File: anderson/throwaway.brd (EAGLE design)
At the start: 45.7 x 30.5 mm, 5 parts

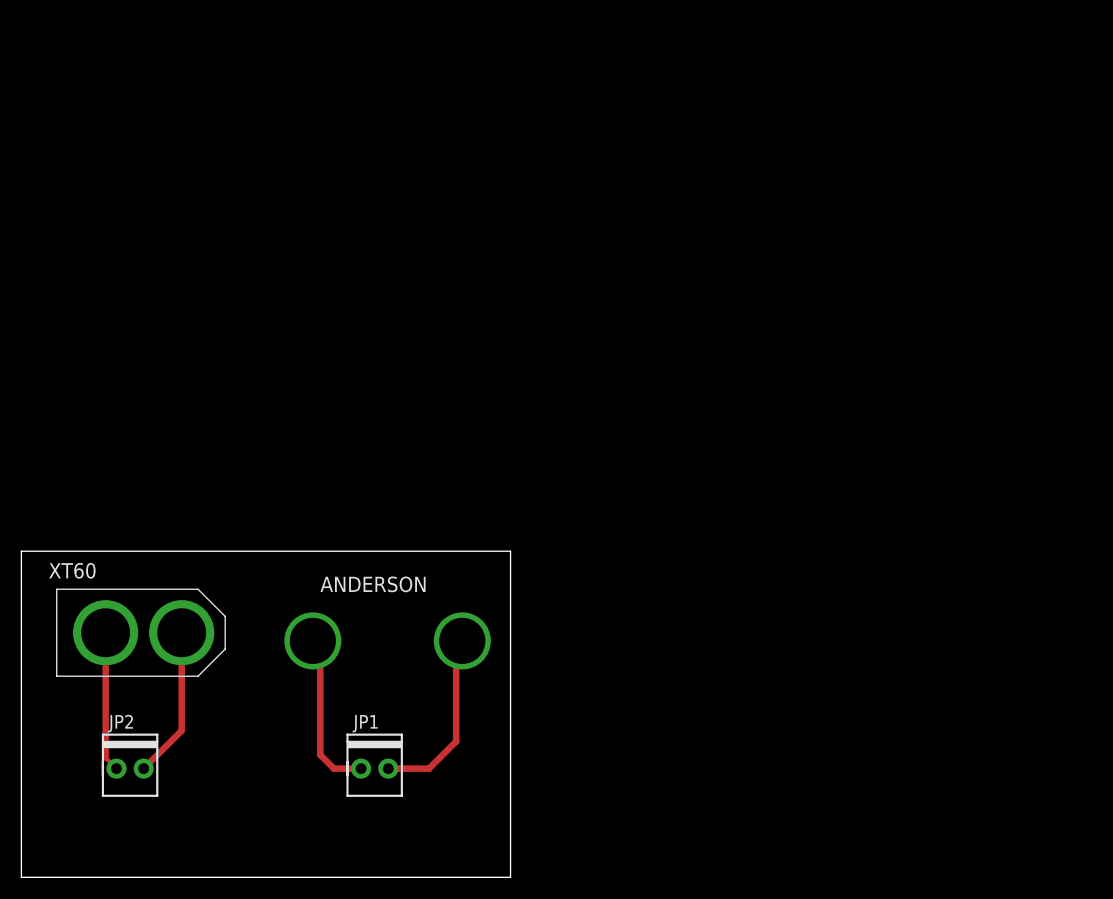
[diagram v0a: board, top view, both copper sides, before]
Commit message: Anderson Throwaways
25 Amp Andersons on throwaway boards with XT60 connectors.
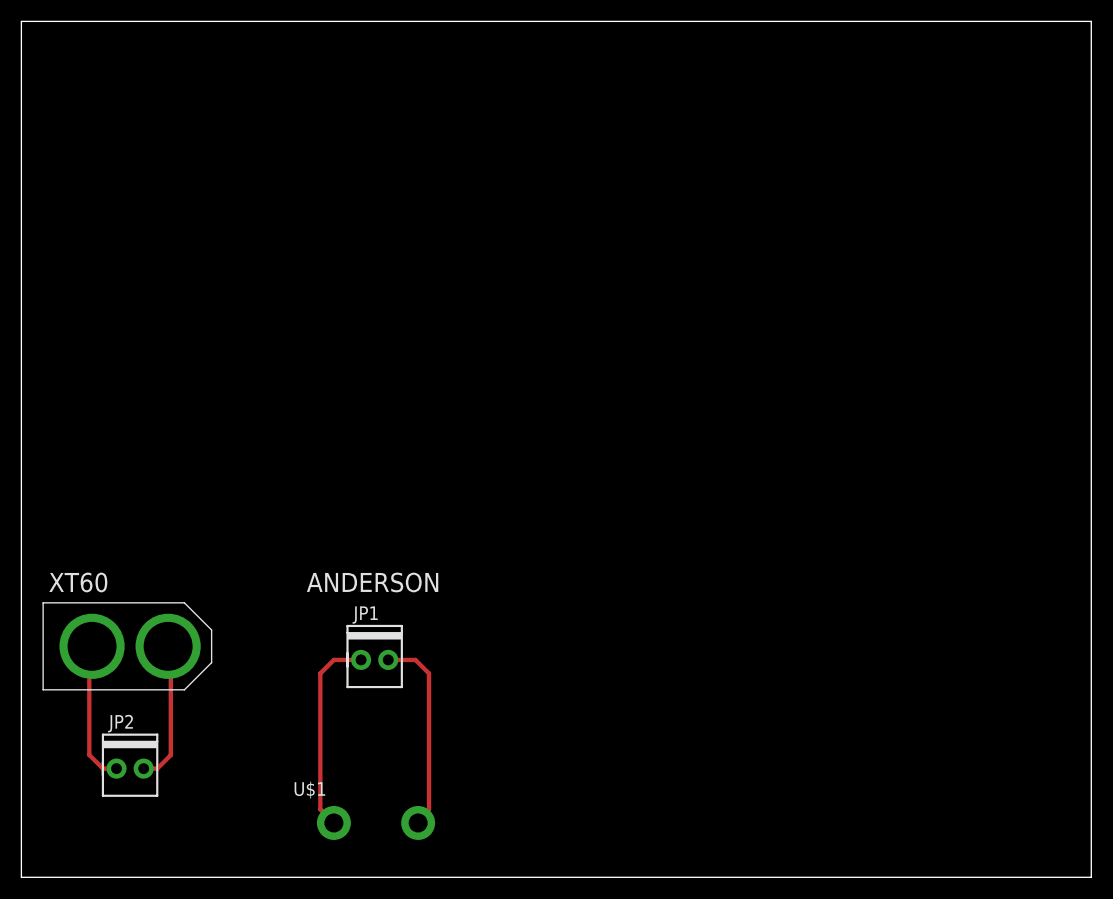
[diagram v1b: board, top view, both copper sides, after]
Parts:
- removed U$2: ANDERSON_RA_BOTTOM, pie:ANDERSON_RA_BOTTOM
- U$1: value ANDERSON_RA_BOTTOM -> ANDERSON_25A_1X2; device pie:ANDERSON_RA_BOTTOM -> pie:ANDERSON_25A_1X2
- moved U$1 16.9 mm to (29.2, 5.08)
- moved JP1 10.2 mm to (33.0, 20.3)
- moved U$3 1.80 mm to (10.2, 21.6)
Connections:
- net N$2: now also U$1.PIN2; no longer U$2.PIN1
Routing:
- net N$1: track 15.3 -> 18.8 mm
- net N$2: track 17.0 -> 18.8 mm
- net N$3: track 14.2 -> 13.2 mm
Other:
- board size 45.7 x 30.5 mm -> 100 x 80 mm

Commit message: Anderson Throwaway
Replaced wrong anderson on throwaway with correct 25A andersons
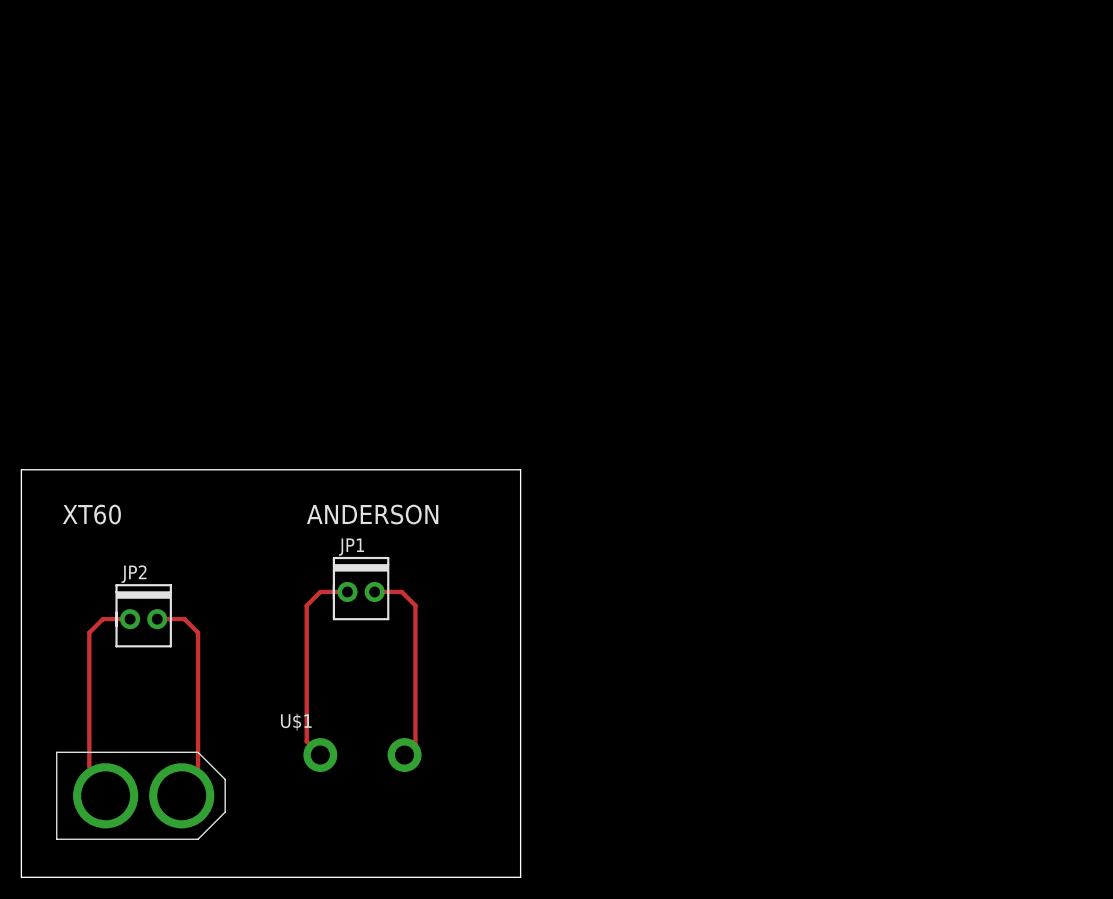
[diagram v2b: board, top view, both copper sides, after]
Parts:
- moved JP2 14.0 mm to (11.4, 24.1)
- moved U$3 14.0 mm to (11.4, 7.62)
- moved JP1 6.48 mm to (31.8, 26.7)
- moved U$1 6.48 mm to (27.9, 11.4)
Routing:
- net N$3: track 13.2 -> 20.2 mm
- net N$4: track 13.2 -> 20.2 mm
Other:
- board size 100 x 80 mm -> 46.7 x 38.1 mm
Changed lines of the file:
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@@
 <board>
 <plain>
-<wire x1="0" y1="0" x2="100" y2="0" width="0" layer="20"/>
-<wire x1="100" y1="0" x2="100" y2="80" width="0" layer="20"/>
-<wire x1="100" y1="80" x2="0" y2="80" width="0" layer="20"/>
-<wire x1="0" y1="80" x2="0" y2="0" width="0" layer="20"/>
-<text x="2.54" y="26.67" size="1.778" layer="25" font="vector">XT60</text>
-<text x="26.67" y="26.67" size="1.778" layer="25" font="vector">ANDERSON</text>
+<wire x1="0" y1="0" x2="46.66" y2="0" width="0" layer="20"/>
+<wire x1="46.66" y1="0" x2="46.66" y2="38.09" width="0" layer="20"/>
+<wire x1="46.66" y1="38.09" x2="0" y2="38.09" width="0" layer="20"/>
+<wire x1="0" y1="38.09" x2="0" y2="0" width="0" layer="20"/>
+<text x="3.81" y="33.02" size="1.778" layer="25" font="vector">XT60</text>
+<text x="26.67" y="33.02" size="1.778" layer="25" font="vector">ANDERSON</text>
 </plain>
 <attributes>
@@
 </autorouter>
 <elements>
-<element name="JP1" library="pie" package="1X02-MTA" value="" x="33.02" y="20.32">
-<attribute name="PARTNUMBER" value="A1921-ND" x="66.04" y="11.43" size="1.778" layer="27" display="off"/>
+<element name="JP1" library="pie" package="1X02-MTA" value="" x="31.75" y="26.67">
+<attribute name="PARTNUMBER" value="A1921-ND" x="64.77" y="17.78" size="1.778" layer="27" display="off"/>
 </element>
-<element name="U$3" library="pie" package="XT60CONNECTOR" value="XT60CONNECTOR" x="10.16" y="21.59">
-<attribute name="PARTNUMBER" value="PRT-10474 " x="31.75" y="-22.86" size="1.778" layer="27" display="off"/>
+<element name="U$3" library="pie" package="XT60CONNECTOR" value="XT60CONNECTOR" x="11.43" y="7.62">
+<attribute name="PARTNUMBER" value="PRT-10474 " x="33.02" y="-36.83" size="1.778" layer="27" display="off"/>
 </element>
-<element name="JP2" library="pie" package="1X02-MTA" value="" x="10.16" y="10.16">
-<attribute name="PARTNUMBER" value="A1921-ND" x="49.53" y="1.27" size="1.778" layer="27" display="off"/>
+<element name="JP2" library="pie" package="1X02-MTA" value="" x="11.43" y="24.13">
+<attribute name="PARTNUMBER" value="A1921-ND" x="50.8" y="15.24" size="1.778" layer="27" display="off"/>
 </element>
-<element name="U$1" library="pie" package="ANDERSON_25A_1X2" value="ANDERSON_25A_1X2" x="29.21" y="5.08"/>
+<element name="U$1" library="pie" package="ANDERSON_25A_1X2" value="ANDERSON_25A_1X2" x="27.94" y="11.43"/>
 </elements>
 <signals>
@@
 <contactref element="U$3" pad="GND"/>
 <contactref element="JP2" pad="2"/>
-<wire x1="11.43" y1="10.16" x2="12.7" y2="10.16" width="0.4064" layer="1"/>
-<wire x1="12.7" y1="10.16" x2="13.97" y2="11.43" width="0.4064" layer="1"/>
-<wire x1="13.97" y1="11.43" x2="13.97" y2="21.59" width="0.4064" layer="1"/>
-<wire x1="13.97" y1="21.59" x2="13.716" y2="21.59" width="0" layer="19" extent="1-1"/>
+<wire x1="12.7" y1="24.13" x2="15.24" y2="24.13" width="0.4064" layer="1"/>
+<wire x1="15.24" y1="24.13" x2="16.51" y2="22.86" width="0.4064" layer="1"/>
+<wire x1="16.51" y1="22.86" x2="16.51" y2="9.144" width="0.4064" layer="1"/>
+<wire x1="16.51" y1="9.144" x2="14.986" y2="7.62" width="0.4064" layer="1"/>
 </signal>
 <signal name="N$4">
 <contactref element="U$3" pad="12V"/>
 <contactref element="JP2" pad="1"/>
-<wire x1="8.89" y1="10.16" x2="7.62" y2="10.16" width="0.4064" layer="1"/>
-<wire x1="7.62" y1="10.16" x2="6.35" y2="11.43" width="0.4064" layer="1"/>
-<wire x1="6.35" y1="11.43" x2="6.35" y2="21.59" width="0.4064" layer="1"/>
-<wire x1="6.35" y1="21.59" x2="6.604" y2="21.59" width="0" layer="19" extent="1-1"/>
+<wire x1="10.16" y1="24.13" x2="7.62" y2="24.13" width="0.4064" layer="1"/>
+<wire x1="7.62" y1="24.13" x2="6.35" y2="22.86" width="0.4064" layer="1"/>
+<wire x1="6.35" y1="22.86" x2="6.35" y2="9.144" width="0.4064" layer="1"/>
+<wire x1="6.35" y1="9.144" x2="7.874" y2="7.62" width="0.4064" layer="1"/>
 </signal>
 <signal name="N$1">
 <contactref element="U$1" pad="PIN1"/>
 <contactref element="JP1" pad="1"/>
-<wire x1="31.75" y1="20.32" x2="29.21" y2="20.32" width="0.4064" layer="1"/>
-<wire x1="29.21" y1="20.32" x2="27.94" y2="19.05" width="0.4064" layer="1"/>
-<wire x1="27.94" y1="19.05" x2="27.94" y2="6.35" width="0.4064" layer="1"/>
-<wire x1="27.94" y1="6.35" x2="29.21" y2="5.08" width="0.4064" layer="1"/>
+<wire x1="30.48" y1="26.67" x2="27.94" y2="26.67" width="0.4064" layer="1"/>
+<wire x1="27.94" y1="26.67" x2="26.67" y2="25.4" width="0.4064" layer="1"/>
+<wire x1="26.67" y1="25.4" x2="26.67" y2="12.7" width="0.4064" layer="1"/>
+<wire x1="26.67" y1="12.7" x2="27.94" y2="11.43" width="0.4064" layer="1"/>
 </signal>
 <signal name="N$2">
 <contactref element="U$1" pad="PIN2"/>
 <contactref element="JP1" pad="2"/>
-<wire x1="34.29" y1="20.32" x2="36.83" y2="20.32" width="0.4064" layer="1"/>
-<wire x1="36.83" y1="20.32" x2="38.1" y2="19.05" width="0.4064" layer="1"/>
-<wire x1="38.1" y1="19.05" x2="38.1" y2="6.35" width="0.4064" layer="1"/>
-<wire x1="38.1" y1="6.35" x2="36.83" y2="5.08" width="0.4064" layer="1"/>
-<wire x1="36.83" y1="5.08" x2="37.084" y2="5.08" width="0" layer="19" extent="1-1"/>
+<wire x1="33.02" y1="26.67" x2="35.56" y2="26.67" width="0.4064" layer="1"/>
+<wire x1="35.56" y1="26.67" x2="36.83" y2="25.4" width="0.4064" layer="1"/>
+<wire x1="36.83" y1="25.4" x2="36.83" y2="12.446" width="0.4064" layer="1"/>
+<wire x1="36.83" y1="12.446" x2="35.814" y2="11.43" width="0.4064" layer="1"/>
 </signal>
 </signals>

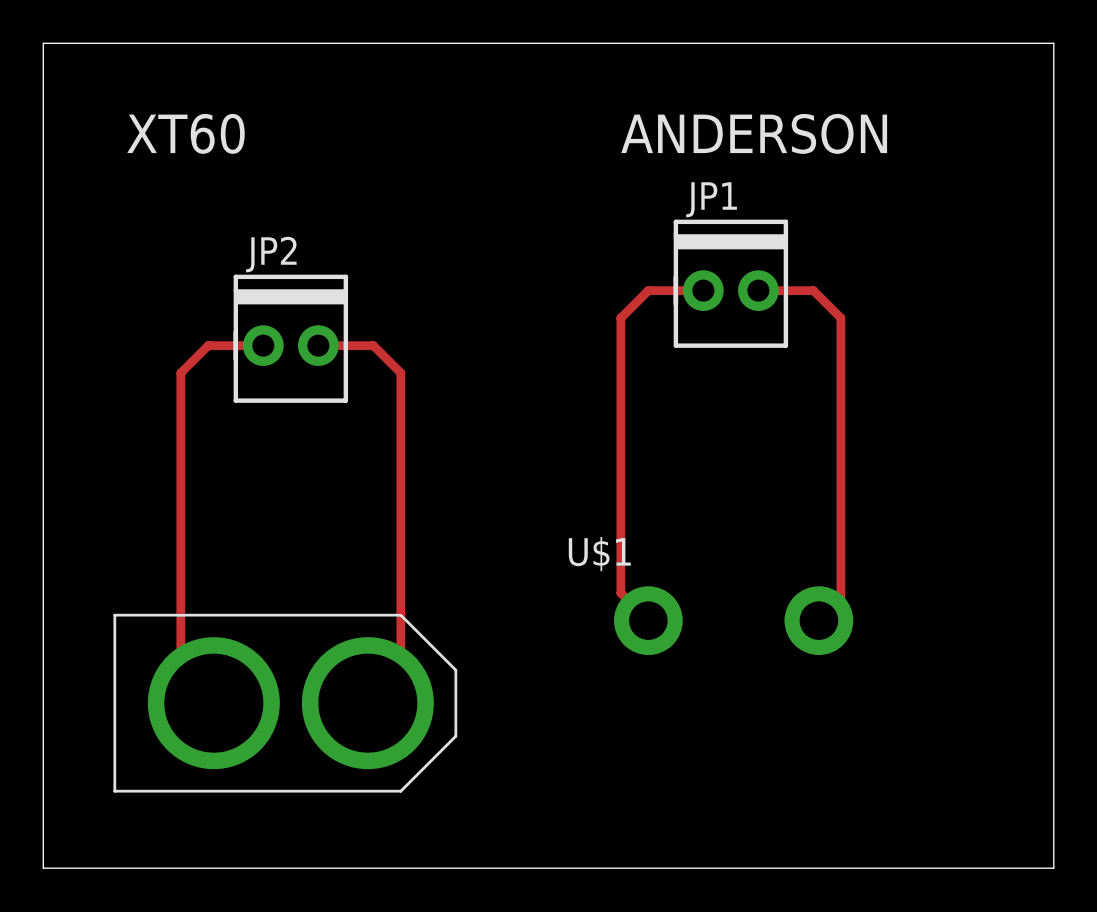
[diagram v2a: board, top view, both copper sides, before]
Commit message: Smaller Throwaway
Compacted the throwaway board to a smaller size
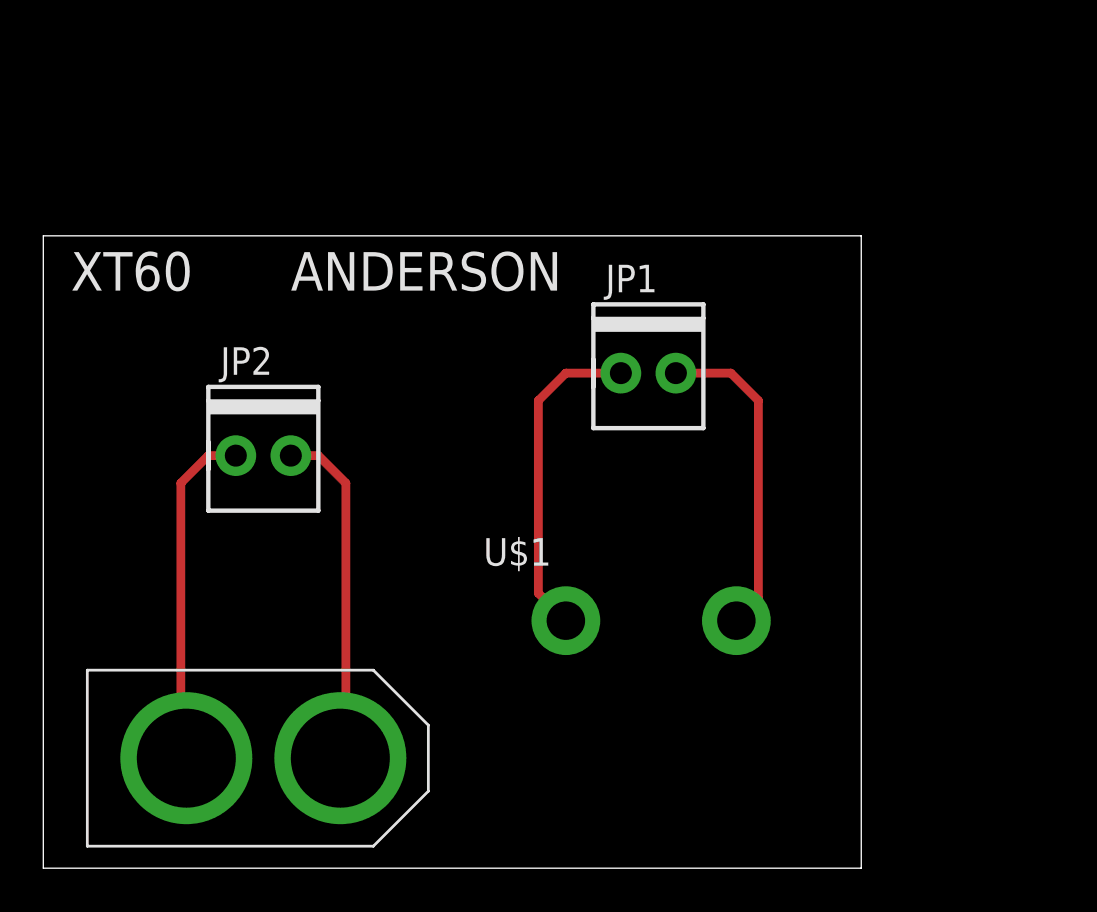
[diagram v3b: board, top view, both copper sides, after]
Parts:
- moved JP1 5.39 mm to (27.9, 22.9)
- moved JP2 5.24 mm to (10.2, 19.1)
- moved U$1 3.81 mm to (24.1, 11.4)
- moved U$3 2.84 mm to (10.2, 5.08)
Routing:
- net N$3: track 20.2 -> 15.9 mm
- net N$4: track 20.2 -> 15.9 mm
- net N$1: track 18.8 -> 15.0 mm
- net N$2: track 18.7 -> 14.9 mm
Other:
- board size 46.7 x 38.1 mm -> 37.8 x 29.2 mm
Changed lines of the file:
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@@
 <board>
 <plain>
-<wire x1="0" y1="0" x2="46.66" y2="0" width="0" layer="20"/>
-<wire x1="46.66" y1="0" x2="46.66" y2="38.09" width="0" layer="20"/>
-<wire x1="46.66" y1="38.09" x2="0" y2="38.09" width="0" layer="20"/>
-<wire x1="0" y1="38.09" x2="0" y2="0" width="0" layer="20"/>
-<text x="3.81" y="33.02" size="1.778" layer="25" font="vector">XT60</text>
-<text x="26.67" y="33.02" size="1.778" layer="25" font="vector">ANDERSON</text>
+<wire x1="0" y1="0" x2="37.77" y2="0" width="0" layer="20"/>
+<wire x1="37.77" y1="0" x2="37.77" y2="29.2" width="0" layer="20"/>
+<wire x1="37.77" y1="29.2" x2="0" y2="29.2" width="0" layer="20"/>
+<wire x1="0" y1="29.2" x2="0" y2="0" width="0" layer="20"/>
+<text x="1.27" y="26.67" size="1.778" layer="25" font="vector">XT60</text>
+<text x="11.43" y="26.67" size="1.778" layer="25" font="vector">ANDERSON</text>
 </plain>
 <attributes>
@@
 </autorouter>
 <elements>
-<element name="JP1" library="pie" package="1X02-MTA" value="" x="31.75" y="26.67">
-<attribute name="PARTNUMBER" value="A1921-ND" x="64.77" y="17.78" size="1.778" layer="27" display="off"/>
+<element name="JP1" library="pie" package="1X02-MTA" value="" x="27.94" y="22.86">
+<attribute name="PARTNUMBER" value="A1921-ND" x="60.96" y="13.97" size="1.778" layer="27" display="off"/>
 </element>
-<element name="U$3" library="pie" package="XT60CONNECTOR" value="XT60CONNECTOR" x="11.43" y="7.62">
-<attribute name="PARTNUMBER" value="PRT-10474 " x="33.02" y="-36.83" size="1.778" layer="27" display="off"/>
+<element name="U$3" library="pie" package="XT60CONNECTOR" value="XT60CONNECTOR" x="10.16" y="5.08">
+<attribute name="PARTNUMBER" value="PRT-10474 " x="31.75" y="-39.37" size="1.778" layer="27" display="off"/>
 </element>
-<element name="JP2" library="pie" package="1X02-MTA" value="" x="11.43" y="24.13">
-<attribute name="PARTNUMBER" value="A1921-ND" x="50.8" y="15.24" size="1.778" layer="27" display="off"/>
+<element name="JP2" library="pie" package="1X02-MTA" value="" x="10.16" y="19.05">
+<attribute name="PARTNUMBER" value="A1921-ND" x="49.53" y="10.16" size="1.778" layer="27" display="off"/>
 </element>
-<element name="U$1" library="pie" package="ANDERSON_25A_1X2" value="ANDERSON_25A_1X2" x="27.94" y="11.43"/>
+<element name="U$1" library="pie" package="ANDERSON_25A_1X2" value="ANDERSON_25A_1X2" x="24.13" y="11.43"/>
 </elements>
 <signals>
@@
 <contactref element="U$3" pad="GND"/>
 <contactref element="JP2" pad="2"/>
-<wire x1="12.7" y1="24.13" x2="15.24" y2="24.13" width="0.4064" layer="1"/>
-<wire x1="15.24" y1="24.13" x2="16.51" y2="22.86" width="0.4064" layer="1"/>
-<wire x1="16.51" y1="22.86" x2="16.51" y2="9.144" width="0.4064" layer="1"/>
-<wire x1="16.51" y1="9.144" x2="14.986" y2="7.62" width="0.4064" layer="1"/>
+<wire x1="11.43" y1="19.05" x2="12.7" y2="19.05" width="0.4064" layer="1"/>
+<wire x1="12.7" y1="19.05" x2="13.97" y2="17.78" width="0.4064" layer="1"/>
+<wire x1="13.97" y1="17.78" x2="13.97" y2="5.334" width="0.4064" layer="1"/>
+<wire x1="13.97" y1="5.334" x2="13.716" y2="5.08" width="0.4064" layer="1"/>
 </signal>
 <signal name="N$4">
 <contactref element="U$3" pad="12V"/>
 <contactref element="JP2" pad="1"/>
-<wire x1="10.16" y1="24.13" x2="7.62" y2="24.13" width="0.4064" layer="1"/>
-<wire x1="7.62" y1="24.13" x2="6.35" y2="22.86" width="0.4064" layer="1"/>
-<wire x1="6.35" y1="22.86" x2="6.35" y2="9.144" width="0.4064" layer="1"/>
-<wire x1="6.35" y1="9.144" x2="7.874" y2="7.62" width="0.4064" layer="1"/>
+<wire x1="8.89" y1="19.05" x2="7.62" y2="19.05" width="0.4064" layer="1"/>
+<wire x1="7.62" y1="19.05" x2="6.35" y2="17.78" width="0.4064" layer="1"/>
+<wire x1="6.35" y1="17.78" x2="6.35" y2="5.334" width="0.4064" layer="1"/>
+<wire x1="6.35" y1="5.334" x2="6.604" y2="5.08" width="0.4064" layer="1"/>
 </signal>
 <signal name="N$1">
 <contactref element="U$1" pad="PIN1"/>
 <contactref element="JP1" pad="1"/>
-<wire x1="30.48" y1="26.67" x2="27.94" y2="26.67" width="0.4064" layer="1"/>
-<wire x1="27.94" y1="26.67" x2="26.67" y2="25.4" width="0.4064" layer="1"/>
-<wire x1="26.67" y1="25.4" x2="26.67" y2="12.7" width="0.4064" layer="1"/>
-<wire x1="26.67" y1="12.7" x2="27.94" y2="11.43" width="0.4064" layer="1"/>
+<wire x1="26.67" y1="22.86" x2="24.13" y2="22.86" width="0.4064" layer="1"/>
+<wire x1="24.13" y1="22.86" x2="22.86" y2="21.59" width="0.4064" layer="1"/>
+<wire x1="22.86" y1="21.59" x2="22.86" y2="12.7" width="0.4064" layer="1"/>
+<wire x1="22.86" y1="12.7" x2="24.13" y2="11.43" width="0.4064" layer="1"/>
 </signal>
 <signal name="N$2">
 <contactref element="U$1" pad="PIN2"/>
 <contactref element="JP1" pad="2"/>
-<wire x1="33.02" y1="26.67" x2="35.56" y2="26.67" width="0.4064" layer="1"/>
-<wire x1="35.56" y1="26.67" x2="36.83" y2="25.4" width="0.4064" layer="1"/>
-<wire x1="36.83" y1="25.4" x2="36.83" y2="12.446" width="0.4064" layer="1"/>
-<wire x1="36.83" y1="12.446" x2="35.814" y2="11.43" width="0.4064" layer="1"/>
+<wire x1="29.21" y1="22.86" x2="31.75" y2="22.86" width="0.4064" layer="1"/>
+<wire x1="31.75" y1="22.86" x2="33.02" y2="21.59" width="0.4064" layer="1"/>
+<wire x1="33.02" y1="21.59" x2="33.02" y2="12.446" width="0.4064" layer="1"/>
+<wire x1="33.02" y1="12.446" x2="32.004" y2="11.43" width="0.4064" layer="1"/>
 </signal>
 </signals>
